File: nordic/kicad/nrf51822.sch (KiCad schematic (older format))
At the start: 17 parts, among them P1 CONN_01X04, P3 CONN_01X01, SW1 SW_Push, U1 BALF-NRF01E3

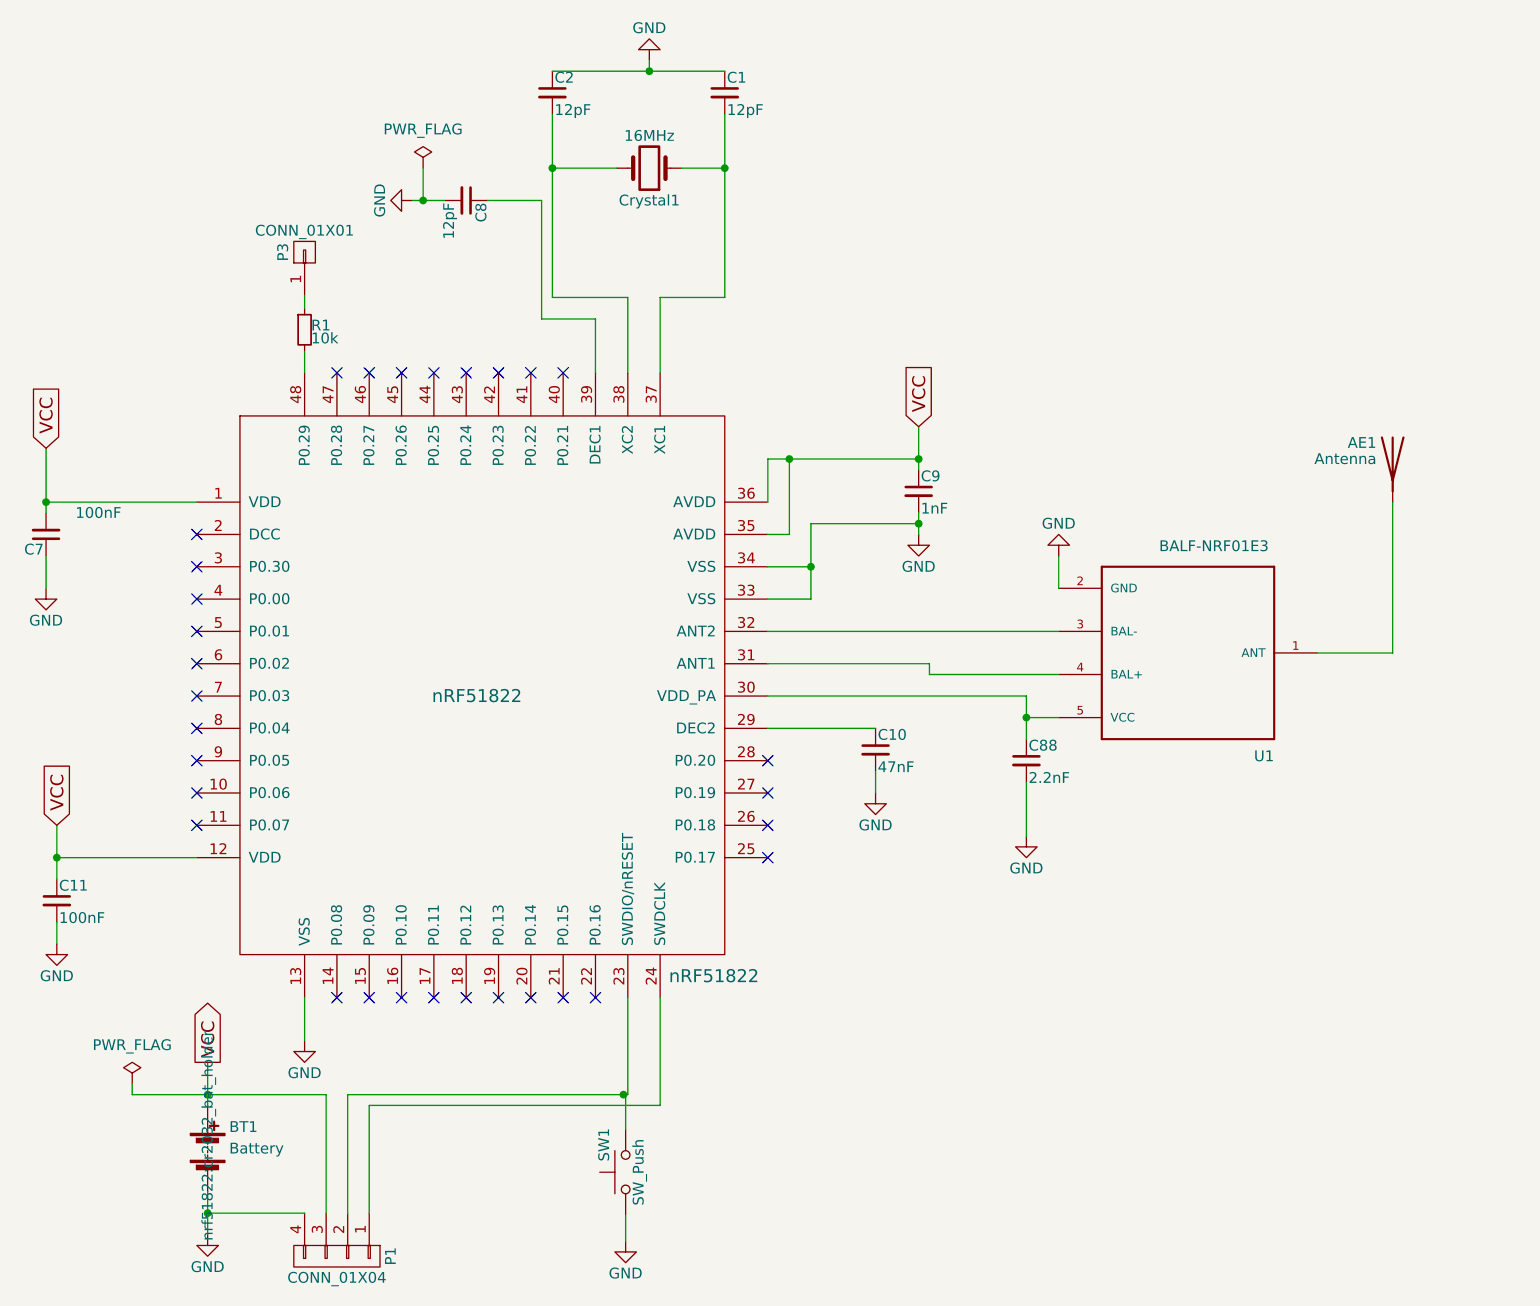
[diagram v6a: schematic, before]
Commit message: Adicionado logo e pino pra Anti-tamper
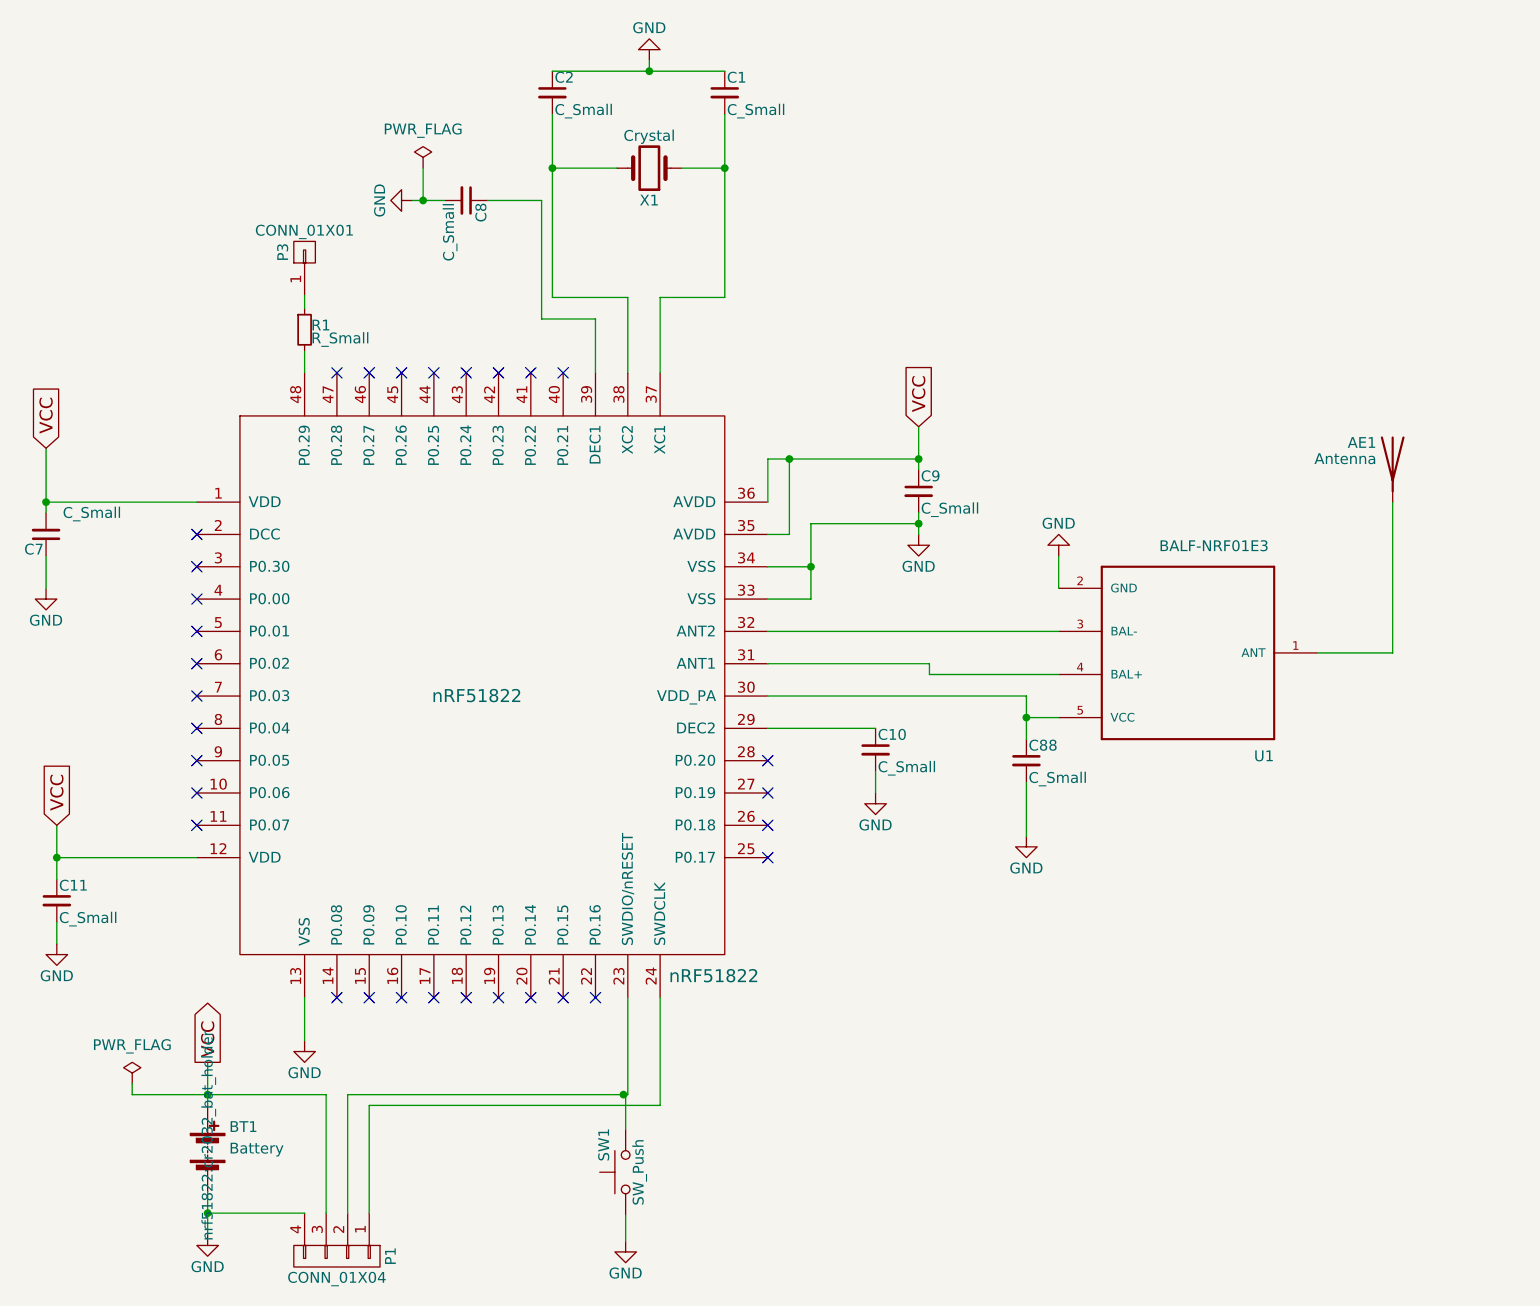
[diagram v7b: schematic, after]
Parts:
- C1, C2, C8: value 12pF -> C_Small
- C10: value 47nF -> C_Small
- C11, C7: value 100nF -> C_Small
- C88: value 2.2nF -> C_Small
- C9: value 1nF -> C_Small
- R1: value 10k -> R_Small
- X1: renamed from Crystal1; value 16MHz -> Crystal
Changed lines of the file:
@@
 $EndDescr
 $Comp
-L GND #PWR01
+L GND #PWR1
 U 1 1 592622FE
 P 3650 3350
-F 0 "#PWR01" H 3650 3100 50  0001 C CNN
+F 0 "#PWR1" H 3650 3100 50  0001 C CNN
 F 1 "GND" H 3650 3200 50  0000 C CNN
 F 2 "" H 3650 3350 50  0000 C CNN
@@
 P 3650 3100
 F 0 "C7" H 3660 3170 50  0000 L CNN
-F 1 "100nF" H 3300 3000 50  0000 L CNN
+F 1 "C_Small" H 3300 3000 50  0000 L CNN
 F 2 "Capacitors_SMD:C_0402" H 3650 3100 50  0001 C CNN
 F 3 "" H 3650 3100 50  0000 C CNN
@@
 P 3700 4800
 F 0 "C11" H 3710 4870 50  0000 L CNN
-F 1 "100nF" H 3710 4720 50  0000 L CNN
+F 1 "C_Small" H 3710 4720 50  0000 L CNN
 F 2 "Capacitors_SMD:C_0402" H 3700 4800 50  0001 C CNN
 F 3 "" H 3700 4800 50  0000 C CNN
@@
 $EndComp
 $Comp
-L GND #PWR02
+L GND #PWR2
 U 1 1 59262909
 P 3700 5000
-F 0 "#PWR02" H 3700 4750 50  0001 C CNN
+F 0 "#PWR2" H 3700 4750 50  0001 C CNN
 F 1 "GND" H 3700 4850 50  0000 C CNN
 F 2 "" H 3700 5000 50  0000 C CNN
@@
 $EndComp
 $Comp
-L GND #PWR03
+L GND #PWR4
 U 1 1 59262B19
 P 4850 5450
-F 0 "#PWR03" H 4850 5200 50  0001 C CNN
+F 0 "#PWR4" H 4850 5200 50  0001 C CNN
 F 1 "GND" H 4850 5300 50  0000 C CNN
 F 2 "" H 4850 5450 50  0000 C CNN
@@
 P 7500 4100
 F 0 "C10" H 7510 4170 50  0000 L CNN
-F 1 "47nF" H 7510 4020 50  0000 L CNN
+F 1 "C_Small" H 7510 4020 50  0000 L CNN
 F 2 "Capacitors_SMD:C_0402" H 7500 4100 50  0001 C CNN
 F 3 "" H 7500 4100 50  0000 C CNN
@@
 $EndComp
 $Comp
-L GND #PWR04
+L GND #PWR8
 U 1 1 59262EC9
 P 7500 4300
-F 0 "#PWR04" H 7500 4050 50  0001 C CNN
+F 0 "#PWR8" H 7500 4050 50  0001 C CNN
 F 1 "GND" H 7500 4150 50  0000 C CNN
 F 2 "" H 7500 4300 50  0000 C CNN
@@
 P 8200 4150
 F 0 "C88" H 8210 4220 50  0000 L CNN
-F 1 "2.2nF" H 8210 4070 50  0000 L CNN
+F 1 "C_Small" H 8210 4070 50  0000 L CNN
 F 2 "Capacitors_SMD:C_0402" H 8200 4150 50  0001 C CNN
 F 3 "" H 8200 4150 50  0000 C CNN
@@
 $EndComp
 $Comp
-L GND #PWR05
+L GND #PWR11
 U 1 1 59262F8A
 P 8350 3200
-F 0 "#PWR05" H 8350 2950 50  0001 C CNN
+F 0 "#PWR11" H 8350 2950 50  0001 C CNN
 F 1 "GND" H 8350 3050 50  0000 C CNN
 F 2 "" H 8350 3200 50  0000 C CNN
@@
 P 7700 2900
 F 0 "C9" H 7710 2970 50  0000 L CNN
-F 1 "1nF" H 7710 2820 50  0000 L CNN
+F 1 "C_Small" H 7710 2820 50  0000 L CNN
 F 2 "Capacitors_SMD:C_0402" H 7700 2900 50  0001 C CNN
 F 3 "" H 7700 2900 50  0000 C CNN
@@
 $EndComp
 $Comp
-L GND #PWR06
+L GND #PWR9
 U 1 1 59263FE2
 P 7700 3100
-F 0 "#PWR06" H 7700 2850 50  0001 C CNN
+F 0 "#PWR9" H 7700 2850 50  0001 C CNN
 F 1 "GND" H 7700 2950 50  0000 C CNN
 F 2 "" H 7700 3100 50  0000 C CNN
@@
 $EndComp
 $Comp
-L Crystal Crystal1
+L Crystal X1
 U 1 1 5926C88D
 P 6450 1400
-F 0 "Crystal1" H 6450 1550 50  0000 C CNN
-F 1 "16MHz" H 6450 1250 50  0000 C CNN
+F 0 "X1" H 6450 1550 50  0000 C CNN
+F 1 "Crystal" H 6450 1250 50  0000 C CNN
 F 2 "Crystals:Crystal_SMD_5032-2pin_5.0x3.2mm" H 6450 1400 50  0001 C CNN
 F 3 "" H 6450 1400 50  0000 C CNN
@@
 $EndComp
 $Comp
-L GND #PWR07
+L GND #PWR7
 U 1 1 5926CA36
 P 6450 900
-F 0 "#PWR07" H 6450 650 50  0001 C CNN
+F 0 "#PWR7" H 6450 650 50  0001 C CNN
 F 1 "GND" H 6450 750 50  0000 C CNN
 F 2 "" H 6450 900 50  0000 C CNN
@@
 P 6000 1050
 F 0 "C2" H 6010 1120 50  0000 L CNN
-F 1 "12pF" H 6010 970 50  0000 L CNN
+F 1 "C_Small" H 6010 970 50  0000 L CNN
 F 2 "Capacitors_SMD:C_0402" H 6000 1050 50  0001 C CNN
 F 3 "" H 6000 1050 50  0000 C CNN
@@
 P 6800 1050
 F 0 "C1" H 6810 1120 50  0000 L CNN
-F 1 "12pF" H 6810 970 50  0000 L CNN
+F 1 "C_Small" H 6810 970 50  0000 L CNN
 F 2 "Capacitors_SMD:C_0402" H 6800 1050 50  0001 C CNN
 F 3 "" H 6800 1050 50  0000 C CNN
@@
 P 5600 1550
 F 0 "C8" H 5610 1620 50  0000 L CNN
-F 1 "12pF" H 5610 1470 50  0000 L CNN
+F 1 "C_Small" H 5610 1470 50  0000 L CNN
 F 2 "Capacitors_SMD:C_0402" H 5600 1550 50  0001 C CNN
 F 3 "" H 5600 1550 50  0000 C CNN
@@
 $EndComp
 $Comp
-L GND #PWR08
+L GND #PWR5
 U 1 1 5926D2E6
 P 5350 1550
-F 0 "#PWR08" H 5350 1300 50  0001 C CNN
+F 0 "#PWR5" H 5350 1300 50  0001 C CNN
 F 1 "GND" H 5350 1400 50  0000 C CNN
 F 2 "" H 5350 1550 50  0000 C CNN
@@
 NoConn ~ 5300 5250
 $Comp
-L PWR_FLAG #FLG09
+L PWR_FLAG #FLG1
 U 1 1 5928F042
 P 4050 5650
-F 0 "#FLG09" H 4050 5745 50  0001 C CNN
+F 0 "#FLG1" H 4050 5745 50  0001 C CNN
 F 1 "PWR_FLAG" H 4050 5830 50  0000 C CNN
 F 2 "" H 4050 5650 50  0000 C CNN
@@
 	4050 5650 4050 5700
 $Comp
-L PWR_FLAG #FLG010
+L PWR_FLAG #FLG2
 U 1 1 5929067A
 P 5400 1400
-F 0 "#FLG010" H 5400 1495 50  0001 C CNN
+F 0 "#FLG2" H 5400 1495 50  0001 C CNN
 F 1 "PWR_FLAG" H 5400 1580 50  0000 C CNN
 F 2 "" H 5400 1400 50  0000 C CNN
@@
 Connection ~ 5400 1550
 $Comp
-L GND #PWR011
+L GND #PWR3
 U 1 1 5929080D
 P 4400 6350
-F 0 "#PWR011" H 4400 6100 50  0001 C CNN
+F 0 "#PWR3" H 4400 6100 50  0001 C CNN
 F 1 "GND" H 4400 6200 50  0000 C CNN
 F 2 "" H 4400 6350 50  0000 C CNN
@@
 Connection ~ 8200 3950
 $Comp
-L GND #PWR012
+L GND #PWR10
 U 1 1 592B023F
 P 8200 4500
-F 0 "#PWR012" H 8200 4250 50  0001 C CNN
+F 0 "#PWR10" H 8200 4250 50  0001 C CNN
 F 1 "GND" H 8200 4350 50  0000 C CNN
 F 2 "" H 8200 4500 50  0000 C CNN
@@
 Connection ~ 6330 5700
 $Comp
-L GND #PWR013
+L GND #PWR6
 U 1 1 593992D9
 P 6340 6380
-F 0 "#PWR013" H 6340 6130 50  0001 C CNN
+F 0 "#PWR6" H 6340 6130 50  0001 C CNN
 F 1 "GND" H 6340 6230 50  0000 C CNN
 F 2 "" H 6340 6380 50  0000 C CNN
@@
 P 4850 2150
 F 0 "R1" H 4880 2170 50  0000 L CNN
-F 1 "10k" H 4880 2110 50  0000 L CNN
+F 1 "R_Small" H 4880 2110 50  0000 L CNN
 F 2 "Resistors_SMD:R_0402" H 4850 2150 50  0001 C CNN
 F 3 "" H 4850 2150 50  0000 C CNN

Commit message: Adicionado componentes 3D
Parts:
- P1: footprint Pin_Headers:Pin_Header_Straight_1x04_Pitch2.00mm -> Pin_Headers:Pin_Header_Straight_1x04_Pitch2.54mm
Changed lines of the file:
@@
 LIBS:BALF-NRF01E3
 LIBS:switches
+LIBS:ESP8266
 LIBS:nrf51822-cache
 EELAYER 25 0
@@
 $EndDescr
 $Comp
-L GND #PWR1
+L GND #PWR01
 U 1 1 592622FE
 P 3650 3350
-F 0 "#PWR1" H 3650 3100 50  0001 C CNN
+F 0 "#PWR01" H 3650 3100 50  0001 C CNN
 F 1 "GND" H 3650 3200 50  0000 C CNN
 F 2 "" H 3650 3350 50  0000 C CNN
@@
 $EndComp
 $Comp
-L GND #PWR2
+L GND #PWR02
 U 1 1 59262909
 P 3700 5000
-F 0 "#PWR2" H 3700 4750 50  0001 C CNN
+F 0 "#PWR02" H 3700 4750 50  0001 C CNN
 F 1 "GND" H 3700 4850 50  0000 C CNN
 F 2 "" H 3700 5000 50  0000 C CNN
@@
 $EndComp
 $Comp
-L GND #PWR4
+L GND #PWR03
 U 1 1 59262B19
 P 4850 5450
-F 0 "#PWR4" H 4850 5200 50  0001 C CNN
+F 0 "#PWR03" H 4850 5200 50  0001 C CNN
 F 1 "GND" H 4850 5300 50  0000 C CNN
 F 2 "" H 4850 5450 50  0000 C CNN
@@
 $EndComp
 $Comp
-L GND #PWR8
+L GND #PWR04
 U 1 1 59262EC9
 P 7500 4300
-F 0 "#PWR8" H 7500 4050 50  0001 C CNN
+F 0 "#PWR04" H 7500 4050 50  0001 C CNN
 F 1 "GND" H 7500 4150 50  0000 C CNN
 F 2 "" H 7500 4300 50  0000 C CNN
@@
 $EndComp
 $Comp
-L GND #PWR11
+L GND #PWR05
 U 1 1 59262F8A
 P 8350 3200
-F 0 "#PWR11" H 8350 2950 50  0001 C CNN
+F 0 "#PWR05" H 8350 2950 50  0001 C CNN
 F 1 "GND" H 8350 3050 50  0000 C CNN
 F 2 "" H 8350 3200 50  0000 C CNN
@@
 $EndComp
 $Comp
-L GND #PWR9
+L GND #PWR06
 U 1 1 59263FE2
 P 7700 3100
-F 0 "#PWR9" H 7700 2850 50  0001 C CNN
+F 0 "#PWR06" H 7700 2850 50  0001 C CNN
 F 1 "GND" H 7700 2950 50  0000 C CNN
 F 2 "" H 7700 3100 50  0000 C CNN
@@
 $EndComp
 $Comp
-L GND #PWR7
+L GND #PWR07
 U 1 1 5926CA36
 P 6450 900
-F 0 "#PWR7" H 6450 650 50  0001 C CNN
+F 0 "#PWR07" H 6450 650 50  0001 C CNN
 F 1 "GND" H 6450 750 50  0000 C CNN
 F 2 "" H 6450 900 50  0000 C CNN
@@
 $EndComp
 $Comp
-L GND #PWR5
+L GND #PWR08
 U 1 1 5926D2E6
 P 5350 1550
-F 0 "#PWR5" H 5350 1300 50  0001 C CNN
+F 0 "#PWR08" H 5350 1300 50  0001 C CNN
 F 1 "GND" H 5350 1400 50  0000 C CNN
 F 2 "" H 5350 1550 50  0000 C CNN
@@
 NoConn ~ 5300 5250
 $Comp
-L PWR_FLAG #FLG1
+L PWR_FLAG #FLG09
 U 1 1 5928F042
 P 4050 5650
-F 0 "#FLG1" H 4050 5745 50  0001 C CNN
+F 0 "#FLG09" H 4050 5745 50  0001 C CNN
 F 1 "PWR_FLAG" H 4050 5830 50  0000 C CNN
 F 2 "" H 4050 5650 50  0000 C CNN
@@
 	4050 5650 4050 5700
 $Comp
-L PWR_FLAG #FLG2
+L PWR_FLAG #FLG010
 U 1 1 5929067A
 P 5400 1400
-F 0 "#FLG2" H 5400 1495 50  0001 C CNN
+F 0 "#FLG010" H 5400 1495 50  0001 C CNN
 F 1 "PWR_FLAG" H 5400 1580 50  0000 C CNN
 F 2 "" H 5400 1400 50  0000 C CNN
@@
 Connection ~ 5400 1550
 $Comp
-L GND #PWR3
+L GND #PWR011
 U 1 1 5929080D
 P 4400 6350
-F 0 "#PWR3" H 4400 6100 50  0001 C CNN
+F 0 "#PWR011" H 4400 6100 50  0001 C CNN
 F 1 "GND" H 4400 6200 50  0000 C CNN
 F 2 "" H 4400 6350 50  0000 C CNN
@@
 F 0 "P1" H 5000 6700 50  0000 C CNN
 F 1 "CONN_01X04" V 5100 6450 50  0000 C CNN
-F 2 "Pin_Headers:Pin_Header_Straight_1x04_Pitch2.00mm" H 5000 6450 50  0001 C CNN
+F 2 "Pin_Headers:Pin_Header_Straight_1x04_Pitch2.54mm" H 5000 6450 50  0001 C CNN
 F 3 "" H 5000 6450 50  0000 C CNN
 	1    5000 6450
@@
 Connection ~ 8200 3950
 $Comp
-L GND #PWR10
+L GND #PWR012
 U 1 1 592B023F
 P 8200 4500
-F 0 "#PWR10" H 8200 4250 50  0001 C CNN
+F 0 "#PWR012" H 8200 4250 50  0001 C CNN
 F 1 "GND" H 8200 4350 50  0000 C CNN
 F 2 "" H 8200 4500 50  0000 C CNN
@@
 Connection ~ 6330 5700
 $Comp
-L GND #PWR6
+L GND #PWR013
 U 1 1 593992D9
 P 6340 6380
-F 0 "#PWR6" H 6340 6130 50  0001 C CNN
+F 0 "#PWR013" H 6340 6130 50  0001 C CNN
 F 1 "GND" H 6340 6230 50  0000 C CNN
 F 2 "" H 6340 6380 50  0000 C CNN
